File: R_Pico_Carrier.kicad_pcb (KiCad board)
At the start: 2 copper layers, 30 parts, among them J1 Conn_01x03_Pin, J2 Conn_01x08_Pin, J3 Conn_01x01_Pin, J4 Conn_01x01_Pin, J5 Conn_01x01_Pin, J6 Conn_01x01_Pin, J7 Conn_01x01_Pin, J8 Conn_01x01_Pin, U1 MCP73831-2-OT, U4 CH32V003FxUx

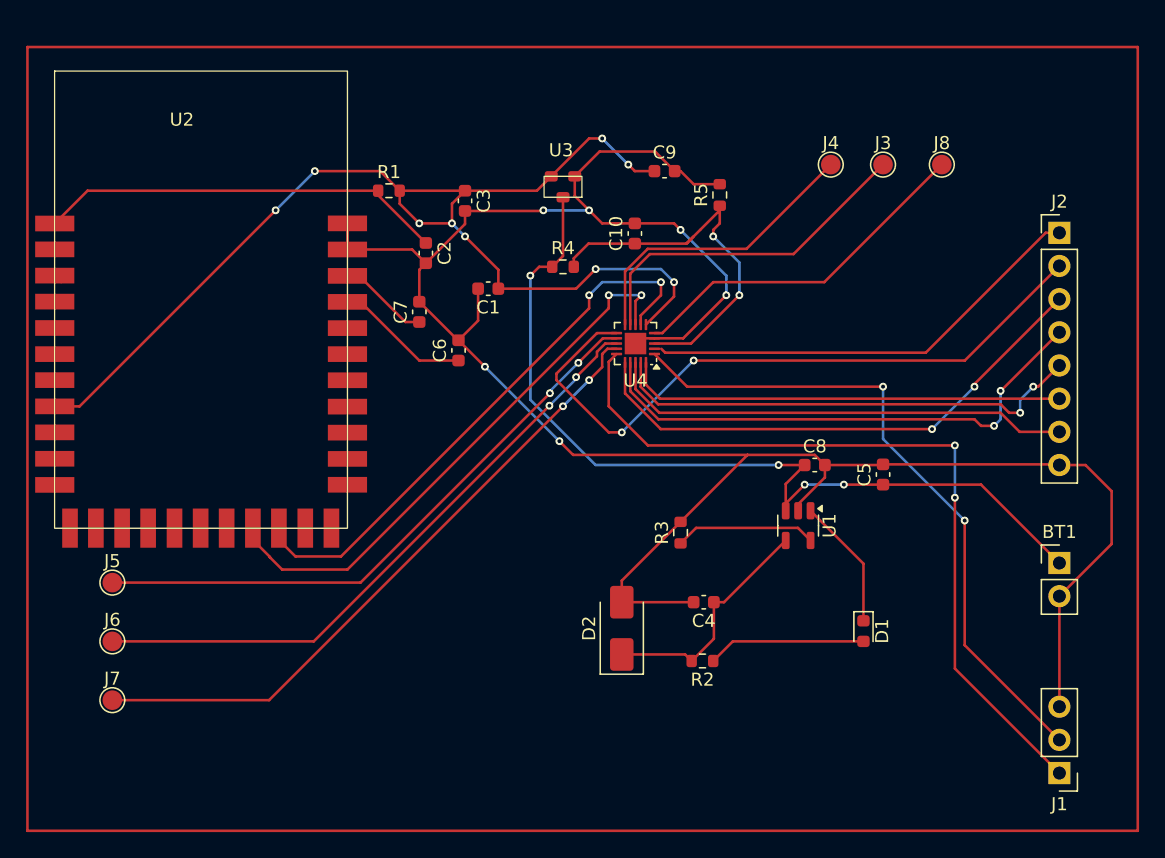
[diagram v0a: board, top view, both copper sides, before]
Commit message: Re-do the board for smaller and tidy palcement
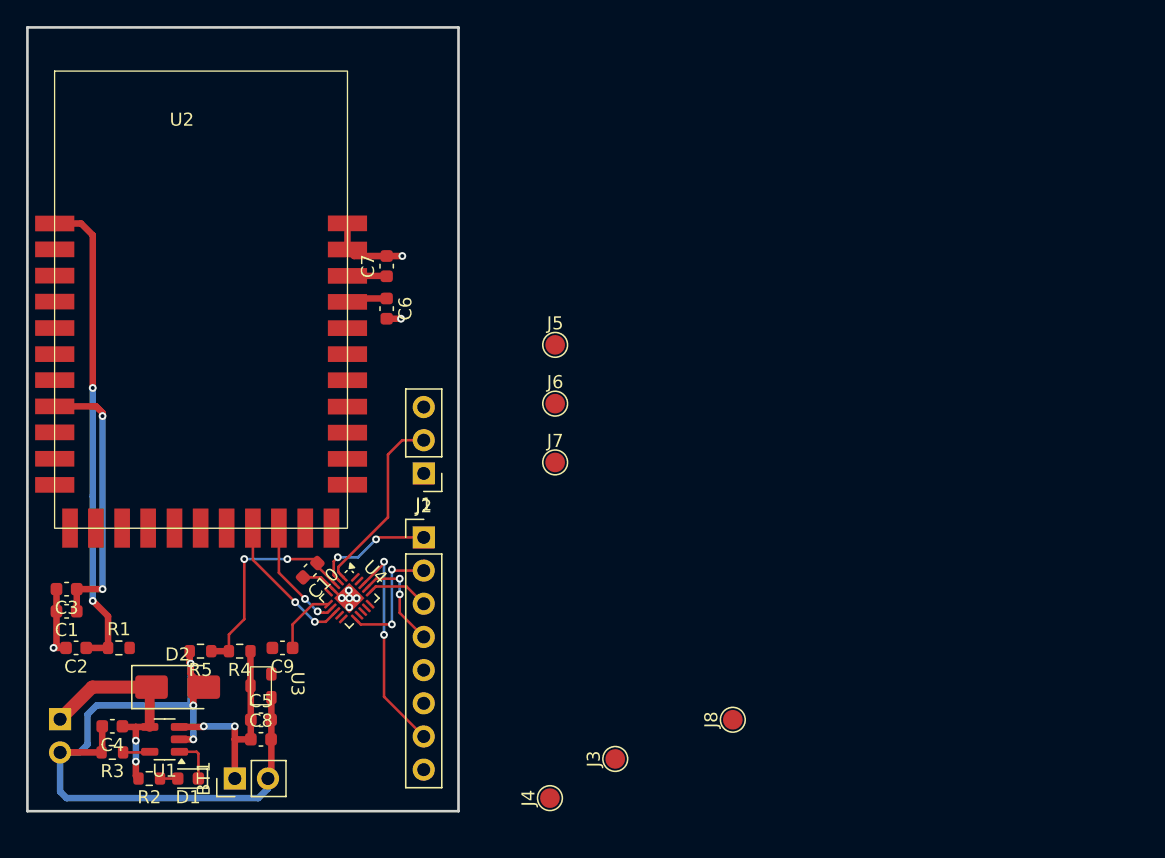
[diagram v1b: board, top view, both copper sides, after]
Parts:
- added J9: Conn_01x02, Connector_PinHeader_2.54mm:PinHeader_1x02_P2.54mm_Vertical, B.Cu at (152.5, 123.0)
- moved BT1 65.2 mm to (165.9, 127.5), turned to 90 degrees
- moved J2 54.0 mm to (180.3, 109.0)
- moved J1 53.8 mm to (180.3, 104.1)
- moved J4 53.1 mm to (190.0, 129.0), turned to 90 degrees
- moved D1 52.9 mm to (162.3, 127.5), turned to 180 degrees
- moved R5 52.9 mm to (163.2, 117.8), turned to 180 degrees
- moved C5 51.2 mm to (167.9, 123.0), turned to 0 degrees
- moved U1 51.2 mm to (160.5, 124.5), turned to 180 degrees
- moved J3 49.9 mm to (195.0, 126.0), turned to 90 degrees
- moved C8 47.3 mm to (167.9, 124.5)
- moved U3 46.9 mm to (168.7, 121.8), turned to 90 degrees
- moved C9 46.8 mm to (169.5, 117.5), turned to 180 degrees
- moved R3 46.6 mm to (156.5, 125.5), turned to 180 degrees
- moved C4 46.3 mm to (156.5, 123.5)
- moved J8 45.4 mm to (204.0, 123.0), turned to 90 degrees
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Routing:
- net GND: track 171.8 -> 75.8 mm, vias 6 -> 11
- net VDD_3V3: track 90.3 -> 26.2 mm, vias 9 -> 2
- net SWIO: track 60.4 -> 0.00 mm, vias 2 -> 0
- net V_Batt: track 68.9 -> 16.2 mm, vias 4 -> 2
- net Spare_5: track 50.3 -> 0.00 mm, vias 2 -> 0
- net Spare_4: track 48.3 -> 0.00 mm, vias 2 -> 0
- net Spare_3: track 46.4 -> 0.00 mm, vias 2 -> 0
- net FSR2_ADC: track 51.8 -> 9.65 mm
- net FSR5_ADC: track 36.9 -> 0.00 mm, vias 2 -> 0
- net nRST: track 51.2 -> 14.3 mm, vias 2 -> 0
- net FSR3_ADC: track 41.0 -> 4.83 mm, vias 2 -> 0
- net UART_TX: track 43.9 -> 8.92 mm
- net FSR6_ADC: track 33.8 -> 0.00 mm
- net FSR4_ADC: track 40.4 -> 8.08 mm
- net UART_RX: track 43.3 -> 11.1 mm
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- added copper zone on B.Cu, net GND
- added copper zone on F.Cu, net VDD_3V3
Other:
- board outline added: 33 x 60 mm
